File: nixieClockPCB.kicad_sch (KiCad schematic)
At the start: 23 parts, among them M1 1364_HV, U1 74141, U10 WeMos_D1_mini, U2 74141, U3 74141, U4 74141, U5 74141, U6 74141, U7 74AHC595, U8 74AHC595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

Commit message: layout moving.
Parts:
- removed M1: 1364_HV, Nixie_footprint_lib:1364_HV, symbol DCDC:1364_HV
- added M2: Nch8200hv, Nixie_footprint_lib:Nch8200hv, symbol nixieclock_project_lib:Nch8200hv
- U1, U2, U3, U4, U5, U6: footprint Package_DIP:DIP-16_W7.62mm_LongPads -> Package_DIP:DIP-16_W7.62mm
- U7, U8, U9: footprint Package_DIP:DIP-16_W7.62mm_LongPads -> nixiemisc:nixiemisc-SOIC16-5.3MM
- renumbered U10 to M1
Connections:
- net +5V: now also M2.1 (V_IN)
- net GND: now also M2.3 (GND), M2.4 (GND)
- net Vdrive: now also M2.2 (V_OUT)
- net N3_A: now reaches U3.3 (A)
- net N3_A: now also U8.15 (QA)
- net N3_D: now reaches U3.4 (D)
- net N3_D: now also U8.3 (QD)
- net N3_B: now reaches U3.6 (B)
- net N3_B: now also U8.1 (QB)
- net N3_C: now reaches U3.7 (C)
- net N3_C: now also U8.2 (QC)
- net N4_A: now reaches U8.4 (QE)
- net N4_A: now also U4.3 (A)
- net N4_B: now reaches U8.5 (QF)
- net N4_B: now also U4.6 (B)
- net N4_C: now reaches U8.6 (QG)
- net N4_C: now also U4.7 (C)
- net N4_D: now reaches U8.7 (QH)
- net N4_D: now also U4.4 (D)
- net N5_B: now reaches U9.1 (QB)
- net N5_B: now also U5.6 (B)
- net N5_A: now reaches U9.15 (QA)
- net N5_A: now also U5.3 (A)
- net N5_C: now reaches U9.2 (QC)
- net N5_C: now also U5.7 (C)
- net N5_D: now reaches U9.3 (QD)
- net N5_D: now also U5.4 (D)
- net N6_A: now reaches U9.4 (QE)
- net N6_A: now also U6.3 (A)
- net N6_B: now reaches U9.5 (QF)
- net N6_B: now also U6.6 (B)
- net N6_C: now reaches U9.6 (QG)
- net N6_C: now also U6.7 (C)
- net N6_D: now reaches U9.7 (QH)
- net N6_D: now also U6.4 (D)
- net N1_A: now reaches U1.3 (A)
- net N1_A: now also U7.15 (QA)
- net N1_D: now reaches U1.4 (D)
- net N1_D: now also U7.3 (QD)
- net N1_B: now reaches U1.6 (B)
- net N1_B: now also U7.1 (QB)
- net N1_C: now reaches U1.7 (C)
- net N1_C: now also U7.2 (QC)
- net N2_A: now reaches U7.4 (QE)
- net N2_A: now also U2.3 (A)
- net N2_B: now reaches U7.5 (QF)
- net N2_B: now also U2.6 (B)
- net N2_C: now reaches U7.6 (QG)
- net N2_C: now also U2.7 (C)
- net N2_D: now reaches U7.7 (QH)
- net N2_D: now also U2.4 (D)
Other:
- moved on the sheet: R1, R2, R3

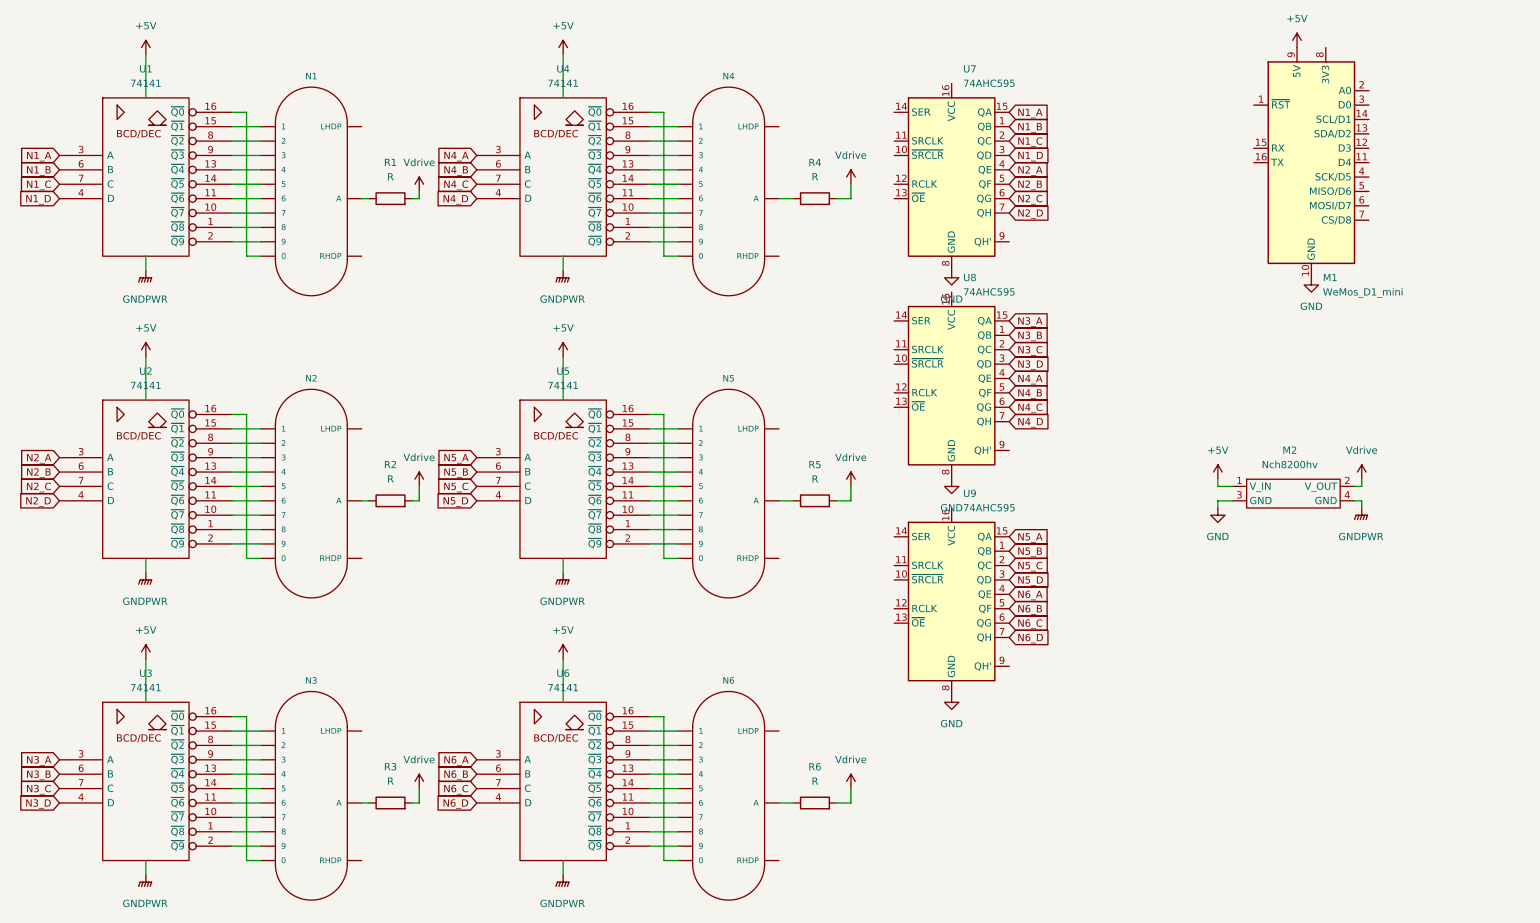
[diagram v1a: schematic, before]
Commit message: First routing iteration done
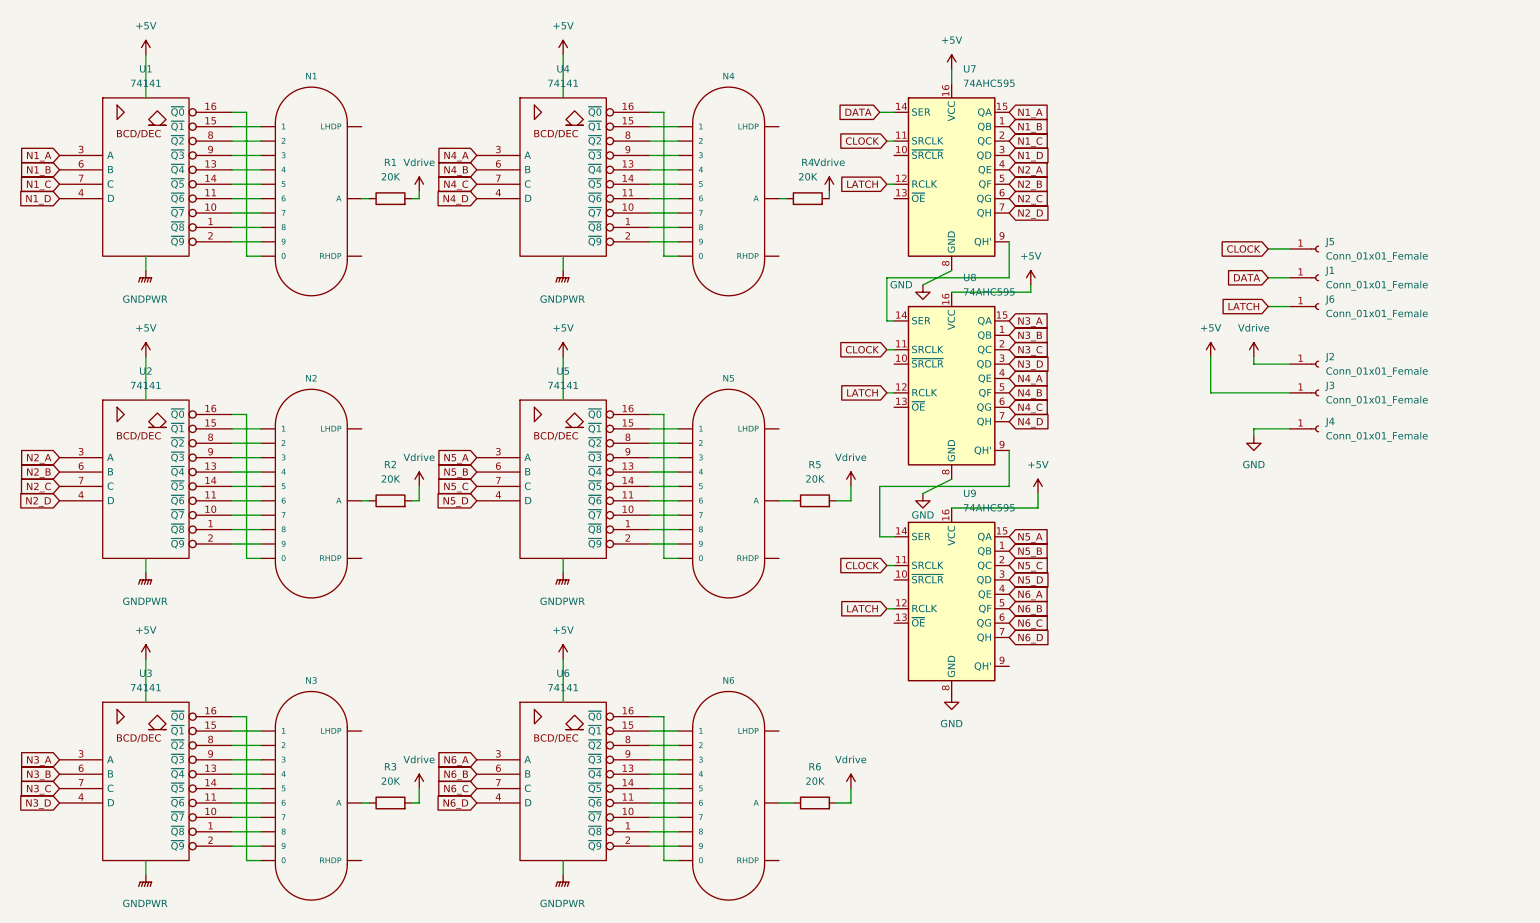
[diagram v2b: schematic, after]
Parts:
- removed M1: WeMos_D1_mini, Module:WEMOS_D1_mini_light, symbol MCU_Module:WeMos_D1_mini
- removed M2: Nch8200hv, Nixie_footprint_lib:Nch8200hv, symbol nixieclock_project_lib:Nch8200hv
- added J1, J2, J3, J4, J5, J6: Conn_01x01_Female, symbol Connector:Conn_01x01_Female
- R1, R2, R3, R4, R5, R6: value R -> 20K; footprint Resistor_THT:R_Axial_DIN0411_L9.9mm_D3.6mm_P12.70mm_Horizontal -> Resistor_THT:R_Axial_DIN0414_L11.9mm_D4.5mm_P15.24mm_Horizontal
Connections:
- net +5V: now also U7.16 (VCC), U8.16 (VCC), U9.16 (VCC), J3.1 (Pin_1)
- net GND: now also J4.1 (Pin_1)
- net Vdrive: now also J2.1 (Pin_1)
- net CLOCK: now reaches U8.11 (SRCLK)
- net CLOCK: now also U7.11 (SRCLK), U9.11 (SRCLK), J5.1 (Pin_1)
- net LATCH: now reaches U8.12 (RCLK)
- net LATCH: now also U7.12 (RCLK), U9.12 (RCLK), J6.1 (Pin_1)
- net at U8.14 (SER): now also U7.9 (QH')
- net at U8.9 (QH'): now also U9.14 (SER)
- net DATA: now reaches U7.14 (SER)
- net DATA: now also J1.1 (Pin_1)
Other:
- moved on the sheet: R4

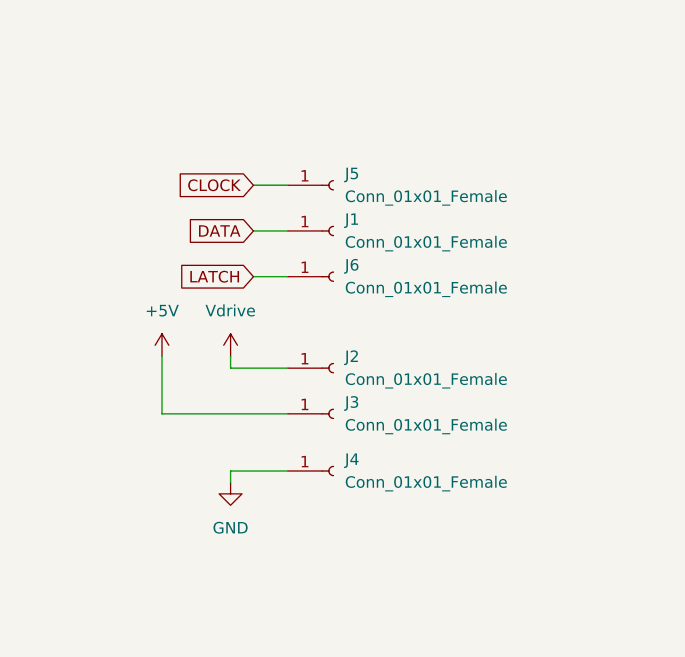
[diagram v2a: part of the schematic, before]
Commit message: Added input
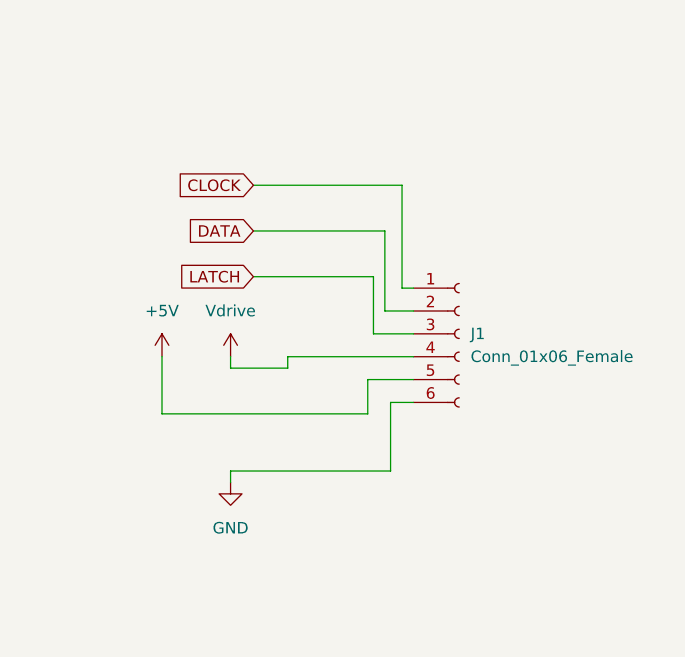
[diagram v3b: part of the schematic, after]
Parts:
- removed J1, J2, J3, J4, J5, J6: Conn_01x01_Female, symbol Connector:Conn_01x01_Female
- added J1: Conn_01x06_Female, Connector_PinHeader_1.27mm:PinHeader_1x06_P1.27mm_Vertical, symbol Connector:Conn_01x06_Female
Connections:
- net +5V: now also J1.5 (Pin_5)
- net CLOCK: now also J1.1 (Pin_1)
- net DATA: now also J1.2 (Pin_2)
- net GND: now also J1.6 (Pin_6)
- net LATCH: now also J1.3 (Pin_3)
- net Vdrive: now also J1.4 (Pin_4)
